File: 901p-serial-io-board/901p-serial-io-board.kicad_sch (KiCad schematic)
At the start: 5 parts, among them J1 DE15, J2 DE9, J3 Barrel Jack, J4 Banana Plug (V+), J5 Banana Plug (V-)

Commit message: new board ooh
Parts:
- removed J2: DE9, symbol Connector:DE9_Pins
- removed J3: Barrel Jack, symbol Connector:Barrel_Jack
- added J2: DE9_Socket, DE9_Amphenol_LD09S24A4GV00LF:AMPHENOL_LD09S24A4GV00LF, symbol Connector:DE9_Socket
- added J3: Barrel_Jack_MountingPin, Barrel_SameSky_PJ-002B:CUI_PJ-002B, symbol Connector:Barrel_Jack_MountingPin
- J1: footprint (none) -> DE15_Amphenol_ICD15S13E4GX00LF:AMPHENOL_ICD15S13E4GX00LF
- J4: value Banana Plug (V+) -> V+; footprint (none) -> Banana_Cinch_105_1102_001:CINCH_105-1102-001
- J5: value Banana Plug (V-) -> V-; footprint (none) -> Banana_Cinch_105_1102_001:CINCH_105-1102-001
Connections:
- net at J1.4, J5.1 (Pin_1): now also J2.9, J3.2, J3.MP (MountPin)
- net at J1.1: now also J2.6
- net at J1.2: now also J2.7
- net at J1.3, J4.1 (Pin_1): now also J3.1
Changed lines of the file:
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@@
+	)
+	(junction
+		(at 45.72 85.09)
+		(diameter 0)
+		(color 0 0 0 0)
 	)
 	(junction
@@
 	(wire
 		(pts
+			(xy 45.72 85.09) (xy 45.72 90.17)
+		)
+		(stroke
+			(width 0)
+			(type default)
+		)
+	)
+	(wire
+		(pts
 			(xy 45.72 45.72) (xy 69.85 45.72)
 		)
@@
 		(pts
 			(xy 45.72 85.09) (xy 62.23 85.09)
+		)
+		(stroke
+			(width 0)
+			(type default)
+		)
+	)
+	(wire
+		(pts
+			(xy 38.1 90.17) (xy 45.72 90.17)
 		)
 		(stroke
@@
 			)
 		)
-		(property "Value" "Banana Plug (V-)"
+		(property "Value" "V-"
 			(at 78.74 86.3599 0)
 			(effects
@@
 			)
 		)
-		(property "Footprint" ""
+		(property "Footprint" "Banana_Cinch_105_1102_001:CINCH_105-1102-001"
 			(at 77.47 85.09 0)
 			(effects
@@
 	)
 	(symbol
-		(lib_id "Connector:DE9_Pins")
-		(at 77.47 50.8 0)
-		(mirror x)
+		(lib_id "Connector:DE9_Socket")
+		(at 77.47 53.34 0)
 		(unit 1)
 		(exclude_from_sim no)
@@
 		(fields_autoplaced yes)
 		(property "Reference" "J2"
-			(at 82.55 52.0701 0)
-			(effects
-				(font
-					(size 1.27 1.27)
-				)
-				(justify left)
-			)
-		)
-		(property "Value" "DE9"
-			(at 82.55 49.5301 0)
-			(effects
-				(font
-					(size 1.27 1.27)
-				)
-				(justify left)
-			)
-		)
-		(property "Footprint" ""
-			(at 77.47 50.8 0)
+			(at 82.55 52.0699 0)
+			(effects
+				(font
+					(size 1.27 1.27)
+				)
+				(justify left)
+			)
+		)
+		(property "Value" "DE9_Socket"
+			(at 82.55 54.6099 0)
+			(effects
+				(font
+					(size 1.27 1.27)
+				)
+				(justify left)
+			)
+		)
+		(property "Footprint" "DE9_Amphenol_LD09S24A4GV00LF:AMPHENOL_LD09S24A4GV00LF"
+			(at 77.47 53.34 0)
 			(effects
 				(font
@@
 		)
 		(property "Datasheet" "~"
-			(at 77.47 50.8 0)
-			(effects
-				(font
-					(size 1.27 1.27)
-				)
-				(hide yes)
-			)
-		)
-		(property "Description" "9-pin D-SUB connector, pins (male)"
-			(at 77.47 50.8 0)
-			(effects
-				(font
-					(size 1.27 1.27)
-				)
-				(hide yes)
-			)
+			(at 77.47 53.34 0)
+			(effects
+				(font
+					(size 1.27 1.27)
+				)
+				(hide yes)
+			)
+		)
+		(property "Description" "9-pin D-SUB connector, socket (female)"
+			(at 77.47 53.34 0)
+			(effects
+				(font
+					(size 1.27 1.27)
+				)
+				(hide yes)
+			)
+		)
+		(pin "4"
+		)
+		(pin "9"
+		)
+		(pin "5"
+		)
+		(pin "1"
+		)
+		(pin "3"
+		)
+		(pin "6"
+		)
+		(pin "2"
+		)
+		(pin "7"
 		)
 		(pin "8"
-		)
-		(pin "3"
-		)
-		(pin "7"
-		)
-		(pin "9"
-		)
-		(pin "5"
-		)
-		(pin "1"
-		)
-		(pin "6"
-		)
-		(pin "2"
-		)
-		(pin "4"
 		)
 		(instances
@@
 	)
 	(symbol
-		(lib_id "Connector:Barrel_Jack")
+		(lib_id "Connector:Barrel_Jack_MountingPin")
 		(at 38.1 82.55 0)
 		(unit 1)
@@
 			)
 		)
-		(property "Value" "Barrel Jack"
+		(property "Value" "Barrel_Jack_MountingPin"
 			(at 38.1 76.2 0)
 			(effects
@@
 			)
 		)
-		(property "Footprint" ""
+		(property "Footprint" "Barrel_SameSky_PJ-002B:CUI_PJ-002B"
 			(at 39.37 83.566 0)
 			(effects
@@
 			)
 		)
-		(property "Description" "DC Barrel Jack"
+		(property "Description" "DC Barrel Jack with a mounting pin"
 			(at 38.1 82.55 0)
 			(effects
@@
 		)
 		(pin "1"
+		)
+		(pin "MP"
 		)
 		(instances
@@
 			)
 		)
-		(property "Footprint" ""
+		(property "Footprint" "DE15_Amphenol_ICD15S13E4GX00LF:AMPHENOL_ICD15S13E4GX00LF"
 			(at 62.23 45.72 0)
 			(effects
@@
 			)
 		)
-		(property "Value" "Banana Plug (V+)"
+		(property "Value" "V+"
 			(at 78.74 81.2799 0)
 			(effects
@@
 			)
 		)
-		(property "Footprint" ""
+		(property "Footprint" "Banana_Cinch_105_1102_001:CINCH_105-1102-001"
 			(at 77.47 80.01 0)
 			(effects

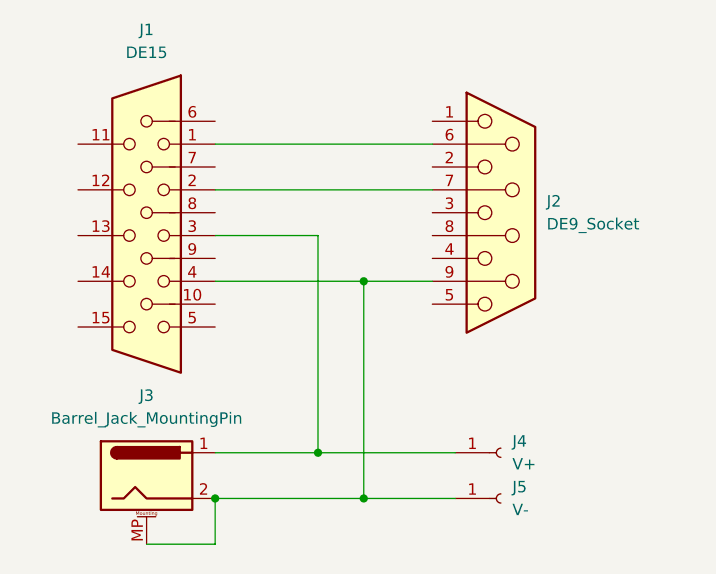
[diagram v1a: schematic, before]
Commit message: fix board pinout, add analog headers
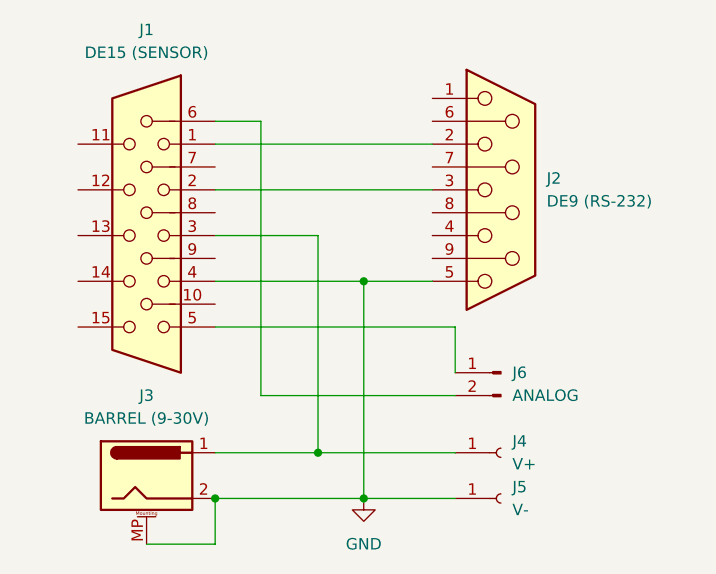
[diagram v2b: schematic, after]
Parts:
- added J6: ANALOG, Connector_PinHeader_2.54mm:PinHeader_1x02_P2.54mm_Vertical, symbol Connector:Conn_01x02_Pin
- J1: value DE15 -> DE15 (SENSOR)
- J2: value DE9_Socket -> DE9 (RS-232)
- J3: value Barrel_Jack_MountingPin -> BARREL (9-30V)
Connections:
- net GND: now reaches J1.4, J3.2, J3.MP (MountPin), J5.1 (Pin_1)
- net GND: now also J2.5; no longer J2.9
- net at J2.2: now also J1.1
- net at J2.3: now also J1.2
- net at J2.6: no longer J1.1
- net at J2.7: no longer J1.2
- net at J1.5: now also J6.1 (Pin_1)
- net at J1.6: now also J6.2 (Pin_2)
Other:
- moved on the sheet: J2
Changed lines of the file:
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@@
+	)
+	(junction
+		(at 62.23 60.96)
+		(diameter 0)
+		(color 0 0 0 0)
 	)
 	(junction
@@
 		(color 0 0 0 0)
 	)
-	(junction
-		(at 62.23 60.96)
-		(diameter 0)
-		(color 0 0 0 0)
+	(wire
+		(pts
+			(xy 50.8 43.18) (xy 50.8 73.66)
+		)
+		(stroke
+			(width 0)
+			(type default)
+		)
 	)
 	(wire
@@
 	(wire
 		(pts
+			(xy 45.72 43.18) (xy 50.8 43.18)
+		)
+		(stroke
+			(width 0)
+			(type default)
+		)
+	)
+	(wire
+		(pts
+			(xy 50.8 73.66) (xy 72.39 73.66)
+		)
+		(stroke
+			(width 0)
+			(type default)
+		)
+	)
+	(wire
+		(pts
+			(xy 57.15 55.88) (xy 45.72 55.88)
+		)
+		(stroke
+			(width 0)
+			(type default)
+		)
+	)
+	(wire
+		(pts
+			(xy 45.72 66.04) (xy 72.39 66.04)
+		)
+		(stroke
+			(width 0)
+			(type default)
+		)
+	)
+	(wire
+		(pts
 			(xy 45.72 45.72) (xy 69.85 45.72)
 		)
@@
 	(wire
 		(pts
-			(xy 57.15 55.88) (xy 45.72 55.88)
-		)
-		(stroke
-			(width 0)
-			(type default)
-		)
-	)
-	(wire
-		(pts
 			(xy 62.23 85.09) (xy 62.23 60.96)
 		)
@@
 	(wire
 		(pts
+			(xy 45.72 85.09) (xy 62.23 85.09)
+		)
+		(stroke
+			(width 0)
+			(type default)
+		)
+	)
+	(wire
+		(pts
+			(xy 38.1 90.17) (xy 45.72 90.17)
+		)
+		(stroke
+			(width 0)
+			(type default)
+		)
+	)
+	(wire
+		(pts
+			(xy 45.72 60.96) (xy 62.23 60.96)
+		)
+		(stroke
+			(width 0)
+			(type default)
+		)
+	)
+	(wire
+		(pts
+			(xy 72.39 66.04) (xy 72.39 71.12)
+		)
+		(stroke
+			(width 0)
+			(type default)
+		)
+	)
+	(wire
+		(pts
+			(xy 57.15 80.01) (xy 57.15 55.88)
+		)
+		(stroke
+			(width 0)
+			(type default)
+		)
+	)
+	(wire
+		(pts
+			(xy 57.15 80.01) (xy 72.39 80.01)
+		)
+		(stroke
+			(width 0)
+			(type default)
+		)
+	)
+	(wire
+		(pts
 			(xy 45.72 50.8) (xy 69.85 50.8)
 		)
@@
 	(wire
 		(pts
-			(xy 45.72 85.09) (xy 62.23 85.09)
-		)
-		(stroke
-			(width 0)
-			(type default)
-		)
-	)
-	(wire
-		(pts
-			(xy 38.1 90.17) (xy 45.72 90.17)
-		)
-		(stroke
-			(width 0)
-			(type default)
-		)
-	)
-	(wire
-		(pts
-			(xy 45.72 60.96) (xy 62.23 60.96)
-		)
-		(stroke
-			(width 0)
-			(type default)
-		)
-	)
-	(wire
-		(pts
-			(xy 57.15 80.01) (xy 57.15 55.88)
-		)
-		(stroke
-			(width 0)
-			(type default)
-		)
-	)
-	(wire
-		(pts
-			(xy 57.15 80.01) (xy 72.39 80.01)
+			(xy 62.23 60.96) (xy 69.85 60.96)
 		)
 		(stroke
@@
 		(pts
 			(xy 45.72 80.01) (xy 57.15 80.01)
-		)
-		(stroke
-			(width 0)
-			(type default)
-		)
-	)
-	(wire
-		(pts
-			(xy 62.23 60.96) (xy 69.85 60.96)
 		)
 		(stroke
@@
 	(symbol
 		(lib_id "Connector:DE9_Socket")
-		(at 77.47 53.34 0)
+		(at 77.47 50.8 0)
 		(unit 1)
 		(exclude_from_sim no)
@@
 		(fields_autoplaced yes)
 		(property "Reference" "J2"
+			(at 82.55 49.5299 0)
+			(effects
+				(font
+					(size 1.27 1.27)
+				)
+				(justify left)
+			)
+		)
+		(property "Value" "DE9 (RS-232)"
 			(at 82.55 52.0699 0)
 			(effects
@@
 			)
 		)
-		(property "Value" "DE9_Socket"
-			(at 82.55 54.6099 0)
-			(effects
-				(font
-					(size 1.27 1.27)
-				)
-				(justify left)
-			)
-		)
 		(property "Footprint" "DE9_Amphenol_LD09S24A4GV00LF:AMPHENOL_LD09S24A4GV00LF"
-			(at 77.47 53.34 0)
+			(at 77.47 50.8 0)
 			(effects
 				(font
@@
 		)
 		(property "Datasheet" "~"
-			(at 77.47 53.34 0)
+			(at 77.47 50.8 0)
 			(effects
 				(font
@@
 		)
 		(property "Description" "9-pin D-SUB connector, socket (female)"
-			(at 77.47 53.34 0)
+			(at 77.47 50.8 0)
 			(effects
 				(font
@@
 				(path "/df698308-057f-440f-9212-28acdb8c5e2b"
 					(reference "J2")
+					(unit 1)
+				)
+			)
+		)
+	)
+	(symbol
+		(lib_id "power:GND")
+		(at 62.23 85.09 0)
+		(unit 1)
+		(exclude_from_sim no)
+		(in_bom yes)
+		(on_board yes)
+		(dnp no)
+		(fields_autoplaced yes)
+		(property "Reference" "#PWR01"
+			(at 62.23 91.44 0)
+			(effects
+				(font
+					(size 1.27 1.27)
+				)
+				(hide yes)
+			)
+		)
+		(property "Value" "GND"
+			(at 62.23 90.17 0)
+			(effects
+				(font
+					(size 1.27 1.27)
+				)
+			)
+		)
+		(property "Footprint" ""
+			(at 62.23 85.09 0)
+			(effects
+				(font
+					(size 1.27 1.27)
+				)
+				(hide yes)
+			)
+		)
+		(property "Datasheet" ""
+			(at 62.23 85.09 0)
+			(effects
+				(font
+					(size 1.27 1.27)
+				)
+				(hide yes)
+			)
+		)
+		(property "Description" "Power symbol creates a global label with name \"GND\" , ground"
+			(at 62.23 85.09 0)
+			(effects
+				(font
+					(size 1.27 1.27)
+				)
+				(hide yes)
+			)
+		)
+		(pin "1"
+		)
+		(instances
+			(project ""
+				(path "/df698308-057f-440f-9212-28acdb8c5e2b"
+					(reference "#PWR01")
+					(unit 1)
+				)
+			)
+		)
+	)
+	(symbol
+		(lib_id "Connector:Conn_01x02_Pin")
+		(at 77.47 71.12 0)
+		(mirror y)
+		(unit 1)
+		(exclude_from_sim no)
+		(in_bom yes)
+		(on_board yes)
+		(dnp no)
+		(fields_autoplaced yes)
+		(property "Reference" "J6"
+			(at 78.74 71.1199 0)
+			(effects
+				(font
+					(size 1.27 1.27)
+				)
+				(justify right)
+			)
+		)
+		(property "Value" "ANALOG"
+			(at 78.74 73.6599 0)
+			(effects
+				(font
+					(size 1.27 1.27)
+				)
+				(justify right)
+			)
+		)
+		(property "Footprint" "Connector_PinHeader_2.54mm:PinHeader_1x02_P2.54mm_Vertical"
+			(at 77.47 71.12 0)
+			(effects
+				(font
+					(size 1.27 1.27)
+				)
+				(hide yes)
+			)
+		)
+		(property "Datasheet" "~"
+			(at 77.47 71.12 0)
+			(effects
+				(font
+					(size 1.27 1.27)
+				)
+				(hide yes)
+			)
+		)
+		(property "Description" "Generic connector, single row, 01x02, script generated"
+			(at 77.47 71.12 0)
+			(effects
+				(font
+					(size 1.27 1.27)
+				)
+				(hide yes)
+			)
+		)
+		(pin "2"
+		)
+		(pin "1"
+		)
+		(instances
+			(project ""
+				(path "/df698308-057f-440f-9212-28acdb8c5e2b"
+					(reference "J6")
 					(unit 1)
 				)
@@
 			)
 		)
-		(property "Value" "Barrel_Jack_MountingPin"
+		(property "Value" "BARREL (9-30V)"
 			(at 38.1 76.2 0)
 			(effects
@@
 			)
 		)
-		(property "Value" "DE15"
+		(property "Value" "DE15 (SENSOR)"
 			(at 38.1 35.56 0)
 			(effects

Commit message: miniaturized board
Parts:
- J2: footprint DE9_Amphenol_LD09S24A4GV00LF:AMPHENOL_LD09S24A4GV00LF -> DE9_Amphenol_LD09S33E4GV00LF:AMPHENOL_LD09S33E4GV00LF
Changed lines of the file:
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@@
 			)
 		)
-		(property "Footprint" "DE9_Amphenol_LD09S24A4GV00LF:AMPHENOL_LD09S24A4GV00LF"
+		(property "Footprint" "DE9_Amphenol_LD09S33E4GV00LF:AMPHENOL_LD09S33E4GV00LF"
 			(at 77.47 50.8 0)
 			(effects
